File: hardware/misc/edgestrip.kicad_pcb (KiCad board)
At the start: 2 copper layers, 6 x 24.1 mm, 2 parts

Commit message: Panelisation stuff
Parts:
- turned REF** to 90 degrees (x2)
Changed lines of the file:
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@@
-(kicad_pcb (version 20200119) (host pcbnew "5.99.0-unknown-9de7547~100~ubuntu18.04.1")
+(kicad_pcb (version 20200119) (host pcbnew "5.99.0-unknown-4f36980~101~ubuntu18.04.1")
   (general
     (thickness 1.6)
@@
       (usegerberadvancedattributes false)
       (creategerberjobfile false)
+      (svguseinch false)
+      (svgprecision 6)
       (excludeedgelayer true)
       (linewidth 0.100000)
@@
   )
   (module "misc:toolhole" (layer "F.Cu")
-    (at 133 82.2)
-    (fp_text reference "REF**" (at 0 2.54 unlocked) (layer "F.SilkS") hide
+    (at 133 82.2 90)
+    (fp_text reference "REF**" (at 0 2.54 90 unlocked) (layer "F.SilkS") hide
       (effects (font (size 1 1) (thickness 0.15)))
     )
-    (fp_text value "toolhole" (at 0 -2.54 unlocked) (layer "F.Fab")
+    (fp_text value "toolhole" (at 0 -2.54 90 unlocked) (layer "F.Fab")
       (effects (font (size 1 1) (thickness 0.15)))
     )
-    (pad "" np_thru_hole circle (at 0 0) (size 1.152 1.152) (drill 1.152) (layers *.Cu *.Mask)
-      (solder_mask_margin 0.148))
+    (fp_text user "tool" (at 0 2 90 unlocked) (layer "F.SilkS")
+      (effects (font (size 1 1) (thickness 0.15)))
+    )
+    (fp_line (start 0 1.6) (end 0 0) (layer "F.SilkS") (width 0.12))
+    (pad "" np_thru_hole circle (at 0 0 90) (size 1.152 1.152) (drill 1.152) (layers *.Cu *.Mask)
+      (solder_mask_margin 0.6))
   )
   (module "misc:toolhole" (layer "F.Cu")
-    (at 133 61.8)
-    (fp_text reference "REF**" (at 0 2.54 unlocked) (layer "F.SilkS") hide
+    (at 133 61.8 90)
+    (fp_text reference "REF**" (at 0 2.54 90 unlocked) (layer "F.SilkS") hide
       (effects (font (size 1 1) (thickness 0.15)))
     )
-    (fp_text value "toolhole" (at 0 -2.54 unlocked) (layer "F.Fab")
+    (fp_text value "toolhole" (at 0 -2.54 90 unlocked) (layer "F.Fab")
       (effects (font (size 1 1) (thickness 0.15)))
     )
-    (pad "" np_thru_hole circle (at 0 0) (size 1.152 1.152) (drill 1.152) (layers *.Cu *.Mask)
-      (solder_mask_margin 0.148))
+    (fp_text user "tool" (at 0 2 90 unlocked) (layer "F.SilkS")
+      (effects (font (size 1 1) (thickness 0.15)))
+    )
+    (fp_line (start 0 1.6) (end 0 0) (layer "F.SilkS") (width 0.12))
+    (pad "" np_thru_hole circle (at 0 0 90) (size 1.152 1.152) (drill 1.152) (layers *.Cu *.Mask)
+      (solder_mask_margin 0.6))
   )
   (gr_text "Order number can be here" (at 132.3 72.6 90) (layer "F.SilkS")

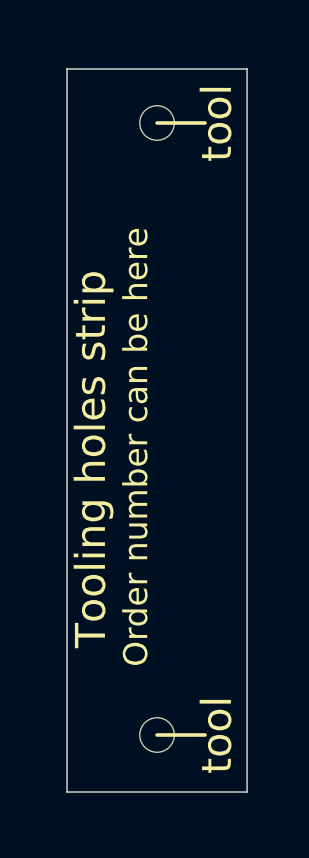
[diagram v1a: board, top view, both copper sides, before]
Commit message: Panelisation changes
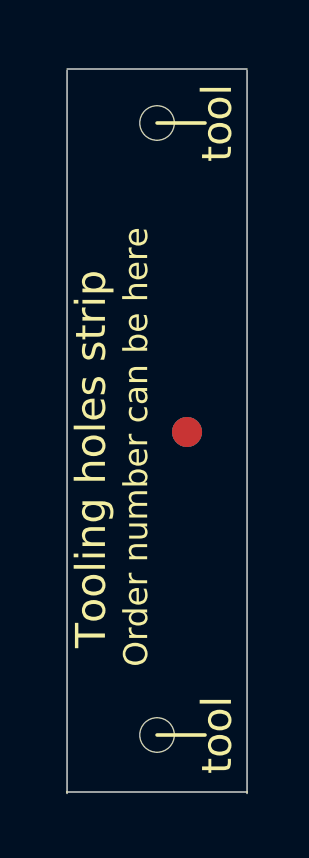
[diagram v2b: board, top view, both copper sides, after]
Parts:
- added REF**: Fiducial_1mm_Mask2mm, Fiducial:Fiducial_1mm_Mask2mm, B.Cu at (134.0, 72.1)
- added REF**: Fiducial_1mm_Mask2mm, Fiducial:Fiducial_1mm_Mask2mm, F.Cu at (134.0, 72.1)
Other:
- board size 6 x 24.1 mm -> 6 x 24.2 mm
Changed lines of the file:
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@@
     (drawings 6)
     (tracks 0)
-    (modules 2)
+    (modules 4)
     (nets 1)
   )
@@
     (solder_mask_min_width 0.25)
     (aux_axis_origin 0 0)
-    (visible_elements FFFDFF7F)
+    (visible_elements FFFDF77F)
     (pcbplotparams
       (layerselection 0x010fc_ffffffff)
@@
     (uvia_drill 0.1)
   )
+  (module "Fiducial:Fiducial_1mm_Mask2mm" (layer "B.Cu")
+    (at 134 72.1)
+    (descr "Circular Fiducial, 1mm bare copper, 2mm soldermask opening (Level A)")
+    (tags "fiducial")
+    (attr smd)
+    (fp_text reference "REF**" (at 0 2) (layer "B.SilkS") hide
+      (effects (font (size 1 1) (thickness 0.15)) (justify mirror))
+    )
+    (fp_text value "Fiducial_1mm_Mask2mm" (at 0 -2) (layer "B.Fab") hide
+      (effects (font (size 1 1) (thickness 0.15)) (justify mirror))
+    )
+    (fp_circle (center 0 0) (end 1.25 0) (layer "B.CrtYd") (width 0.05))
+    (fp_text user "${REFERENCE}" (at 0 0) (layer "B.Fab") hide
+      (effects (font (size 0.4 0.4) (thickness 0.06)) (justify mirror))
+    )
+    (fp_circle (center 0 0) (end 1 0) (layer "B.Fab") (width 0.1))
+    (pad "" smd circle (at 0 0) (size 1 1) (layers "B.Cu" "B.Mask")
+      (solder_mask_margin 0.5) (clearance 0.5))
+  )
+  (module "Fiducial:Fiducial_1mm_Mask2mm" (layer "F.Cu")
+    (at 134 72.1)
+    (descr "Circular Fiducial, 1mm bare copper, 2mm soldermask opening (Level A)")
+    (tags "fiducial")
+    (attr smd)
+    (fp_text reference "REF**" (at 0 -2) (layer "F.SilkS") hide
+      (effects (font (size 1 1) (thickness 0.15)))
+    )
+    (fp_text value "Fiducial_1mm_Mask2mm" (at 0 2) (layer "F.Fab") hide
+      (effects (font (size 1 1) (thickness 0.15)))
+    )
+    (fp_circle (center 0 0) (end 1 0) (layer "F.Fab") (width 0.1))
+    (fp_text user "${REFERENCE}" (at 0 0) (layer "F.Fab") hide
+      (effects (font (size 0.4 0.4) (thickness 0.06)))
+    )
+    (fp_circle (center 0 0) (end 1.25 0) (layer "F.CrtYd") (width 0.05))
+    (pad "" smd circle (at 0 0) (size 1 1) (layers "F.Cu" "F.Mask")
+      (solder_mask_margin 0.5) (clearance 0.5))
+  )
   (module "misc:toolhole" (layer "F.Cu")
     (at 133 82.2 90)
@@
       (effects (font (size 1 1) (thickness 0.15)))
     )
+    (fp_line (start 0 1.6) (end 0 0) (layer "F.SilkS") (width 0.12))
     (fp_text user "tool" (at 0 2 90 unlocked) (layer "F.SilkS")
       (effects (font (size 1 1) (thickness 0.15)))
     )
-    (fp_line (start 0 1.6) (end 0 0) (layer "F.SilkS") (width 0.12))
     (pad "" np_thru_hole circle (at 0 0 90) (size 1.152 1.152) (drill 1.152) (layers *.Cu *.Mask)
       (solder_mask_margin 0.6))
@@
       (effects (font (size 1 1) (thickness 0.15)))
     )
+    (fp_line (start 0 1.6) (end 0 0) (layer "F.SilkS") (width 0.12))
     (fp_text user "tool" (at 0 2 90 unlocked) (layer "F.SilkS")
       (effects (font (size 1 1) (thickness 0.15)))
     )
-    (fp_line (start 0 1.6) (end 0 0) (layer "F.SilkS") (width 0.12))
     (pad "" np_thru_hole circle (at 0 0 90) (size 1.152 1.152) (drill 1.152) (layers *.Cu *.Mask)
       (solder_mask_margin 0.6))
@@
   )
   (gr_line (start 130 84.1) (end 136 84.1) (layer "Edge.Cuts") (width 0.05))
-  (gr_line (start 130 60) (end 130 84.1) (layer "Edge.Cuts") (width 0.05))
-  (gr_line (start 136 60) (end 136 84.1) (layer "Edge.Cuts") (width 0.05))
+  (gr_line (start 130 60.05) (end 130 84.15) (layer "Edge.Cuts") (width 0.05))
+  (gr_line (start 136 60.05) (end 136 84.15) (layer "Edge.Cuts") (width 0.05))
   (gr_line (start 130 60) (end 136 60) (layer "Edge.Cuts") (width 0.05))
 )
